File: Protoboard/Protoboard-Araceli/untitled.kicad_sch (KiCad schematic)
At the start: 23 parts, among them SW1 SW_DIP_x04, SW3 SW_Push, U1 PIC18F4550-IP, U2 HDSP-7803

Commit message: Multiplexed display
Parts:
- removed BAR1: HDSP-4830_2, Display:HDSP-4830, symbol LED:HDSP-4830_2
- removed R1, R2, R3, R4, R5, R6, R7, R8: 330, symbol Device:R
- removed R11, R12, R13, R14, R15, R16, R17: 10k, symbol Device:R
- removed R18: 470, symbol Device:R
- removed R19: 10K, symbol Device:R
- removed SW: SW_DIP_x08, symbol Switch:SW_DIP_x08
- removed SW1: SW_DIP_x04, symbol Switch:SW_DIP_x04
- removed SW3: SW_Push, symbol Switch:SW_Push
- removed U1: PIC18F4550-IP, Package_DIP:DIP-40_W15.24mm, symbol MCU_Microchip_PIC18:PIC18F4550-IP
- removed U2: HDSP-7803, Display_7Segment:HDSP-7801, symbol Display_Character:HDSP-7803
- added BAR2: HDSP-4830_2, Display:HDSP-4830, symbol LED:HDSP-4830_2
- added LEFT, RIght: HDSP-7803, Display_7Segment:HDSP-7801, symbol Display_Character:HDSP-7803
- added R10, R20, R21, R22, R23, R32, R9: 10k, symbol Device:R
- added R24, R25, R26, R27, R28, R29, R30, R31: 330, symbol Device:R
- added R33: 470, symbol Device:R
- added R34: 10K, symbol Device:R
- added SW2: SW_DIP_x04, symbol Switch:SW_DIP_x04
- added SW4: SW_DIP_x08, symbol Switch:SW_DIP_x08
- added SW5: SW_Push, symbol Switch:SW_Push
- added U4: PIC18F4550-IP, Package_DIP:DIP-40_W15.24mm, symbol MCU_Microchip_PIC18:PIC18F4550-IP
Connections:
- net +5V: now also R34.2, SW4.10, SW4.11, SW4.12, SW4.13, SW4.14, SW4.15, SW4.16, SW4.9, U4.11 (VDD)
- net GND: now also R10.2, R20.2, R21.2, R22.2, R23.2, R32.2, R9.2, SW5.2, U4.12 (VSS)
- net MCLR: now also R33.2, R34.1, SW5.1
- net PGC-5: now also R30.2, U4.39 (RB6/KBI2/PGC)
- net PGD-4: now also R31.2, U4.40 (RB7/KBI3/PGD)
- new net: BAR2.7 (A), LEFT.5 (D), R27.1, RIght.5 (D)
- new net: R27.2, U4.36 (RB3/AN9/CCP2/VPO)
- new net: BAR2.6 (A), LEFT.4 (E), R28.1, RIght.4 (E)
- new net: R28.2, U4.37 (RB4/AN11/KBI0/CSSPP)
- new net: BAR2.10 (A), LEFT.10 (A), R24.1, RIght.10 (A)
- new net: BAR2.5 (A), LEFT.2 (F), R29.1, RIght.2 (F)
- new net: BAR2.4 (A), LEFT.3 (G), R30.1, RIght.3 (G)
- new net: LEFT.6 (CC), U4.29 (P1C/SPP6/RD6)
- new net: BAR2.3 (A), LEFT.7 (DP), R31.1
- new net: BAR2.8 (A), LEFT.8 (C), R26.1, RIght.8 (C)
- new net: BAR2.9 (A), LEFT.9 (B), R25.1, RIght.9 (B)
- new net: R9.1, SW4.2, U4.14 (RA6/OSC2/CLKO)
- new net: R10.1, SW4.3, U4.7 (RA5/AN4/~{SS}/HLVDIN/C2OUT)
- new net: R20.1, SW4.4, U4.6 (RA4/T0CKI/C1OUT/RCV)
- new net: R21.1, SW4.5, U4.5 (RA3/AN3/Vref+)
- new net: R22.1, SW4.6, U4.4 (RA2/AN2/Vref-/CVref)
- new net: R23.1, SW4.7, U4.3 (RA1/AN1)
- new net: R32.1, SW4.8, U4.2 (RA0/AN0)
- new net: R26.2, U4.35 (RB2/AN8/INT2/VMO)
- new net: BAR2.11 (K), BAR2.12 (K), BAR2.13 (K), BAR2.14 (K), BAR2.15 (K), BAR2.16 (K), BAR2.17 (K), BAR2.18 (K), BAR2.19 (K), BAR2.20 (K)
- new net: R25.2, U4.34 (RB1/AN10/INT1/SCK/SCL)
- new net: R33.1, U4.1 (Vpp/~{MCLR}/RE3)
- new net: RIght.1 (CC), U4.30 (P1D/SPP7/RD7)
- new net: R24.2, U4.33 (RB0/AN12/INT0/FLT0/SDI/SDA)
- new net: R29.2, U4.38 (RB5/KBI1/PGM)
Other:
- removed sheet Mutiplexed display
- title: Protoboard Araceli -> (none)

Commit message: Last fix
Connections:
- net GND: now also SW2.6
- net at SW2.1: now also RIght.1 (CC)
- net at SW2.2: now also LEFT.6 (CC)
- net at SW2.3: now also BAR2.11 (K), BAR2.12 (K), BAR2.13 (K), BAR2.14 (K), BAR2.15 (K), BAR2.16 (K), BAR2.17 (K), BAR2.18 (K), BAR2.19 (K), BAR2.20 (K)
- net at SW2.7: now also U4.29 (P1C/SPP6/RD6)
- net at SW2.8: now also U4.30 (P1D/SPP7/RD7)
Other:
- moved on the sheet: SW2
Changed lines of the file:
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@@
+	)
+	(junction
+		(at 43.18 116.84)
+		(diameter 0)
+		(color 0 0 0 0)
 	)
 	(junction
@@
 	(wire
 		(pts
-			(xy 231.14 87.63) (xy 231.14 148.59)
-		)
-		(stroke
-			(width 0)
-			(type default)
-		)
-	)
-	(wire
-		(pts
 			(xy 54.61 111.76) (xy 114.3 111.76)
 		)
@@
 	(wire
 		(pts
+			(xy 121.92 140.97) (xy 147.32 140.97)
+		)
+		(stroke
+			(width 0)
+			(type default)
+		)
+	)
+	(wire
+		(pts
 			(xy 72.39 130.81) (xy 67.31 130.81)
 		)
@@
 	(wire
 		(pts
+			(xy 130.81 143.51) (xy 130.81 148.59)
+		)
+		(stroke
+			(width 0)
+			(type default)
+		)
+	)
+	(wire
+		(pts
 			(xy 67.31 130.81) (xy 67.31 99.06)
 		)
@@
 	(wire
 		(pts
+			(xy 162.56 146.05) (xy 171.45 146.05)
+		)
+		(stroke
+			(width 0)
+			(type default)
+		)
+	)
+	(wire
+		(pts
 			(xy 130.81 101.6) (xy 121.92 101.6)
 		)
@@
 	(wire
 		(pts
+			(xy 229.87 143.51) (xy 162.56 143.51)
+		)
+		(stroke
+			(width 0)
+			(type default)
+		)
+	)
+	(wire
+		(pts
 			(xy 101.6 99.06) (xy 114.3 99.06)
 		)
@@
 	(wire
 		(pts
-			(xy 195.58 87.63) (xy 231.14 87.63)
-		)
-		(stroke
-			(width 0)
-			(type default)
-		)
-	)
-	(wire
-		(pts
-			(xy 227.33 140.97) (xy 121.92 140.97)
-		)
-		(stroke
-			(width 0)
-			(type default)
-		)
-	)
-	(wire
-		(pts
 			(xy 99.06 133.35) (xy 99.06 101.6)
 		)
@@
 	(wire
 		(pts
+			(xy 132.08 146.05) (xy 147.32 146.05)
+		)
+		(stroke
+			(width 0)
+			(type default)
+		)
+	)
+	(wire
+		(pts
 			(xy 43.18 101.6) (xy 43.18 104.14)
 		)
@@
 	(wire
 		(pts
-			(xy 231.14 148.59) (xy 87.63 148.59)
+			(xy 43.18 116.84) (xy 43.18 151.13)
 		)
 		(stroke
@@
 	(wire
 		(pts
+			(xy 43.18 151.13) (xy 132.08 151.13)
+		)
+		(stroke
+			(width 0)
+			(type default)
+		)
+	)
+	(wire
+		(pts
 			(xy 53.34 111.76) (xy 54.61 111.76)
 		)
@@
 	(wire
 		(pts
+			(xy 195.58 87.63) (xy 229.87 87.63)
+		)
+		(stroke
+			(width 0)
+			(type default)
+		)
+	)
+	(wire
+		(pts
 			(xy 104.14 96.52) (xy 114.3 96.52)
 		)
@@
 	(wire
 		(pts
-			(xy 128.27 175.26) (xy 128.27 177.8)
-		)
-		(stroke
-			(width 0)
-			(type default)
-		)
-	)
-	(wire
-		(pts
 			(xy 147.32 114.3) (xy 147.32 123.19)
 		)
@@
 	(wire
 		(pts
+			(xy 171.45 146.05) (xy 171.45 148.59)
+		)
+		(stroke
+			(width 0)
+			(type default)
+		)
+	)
+	(wire
+		(pts
+			(xy 130.81 148.59) (xy 87.63 148.59)
+		)
+		(stroke
+			(width 0)
+			(type default)
+		)
+	)
+	(wire
+		(pts
+			(xy 147.32 143.51) (xy 130.81 143.51)
+		)
+		(stroke
+			(width 0)
+			(type default)
+		)
+	)
+	(wire
+		(pts
 			(xy 53.34 96.52) (xy 69.85 96.52)
 		)
@@
 	(wire
 		(pts
+			(xy 229.87 87.63) (xy 229.87 143.51)
+		)
+		(stroke
+			(width 0)
+			(type default)
+		)
+	)
+	(wire
+		(pts
+			(xy 132.08 151.13) (xy 132.08 146.05)
+		)
+		(stroke
+			(width 0)
+			(type default)
+		)
+	)
+	(wire
+		(pts
 			(xy 165.1 110.49) (xy 165.1 118.11)
+		)
+		(stroke
+			(width 0)
+			(type default)
+		)
+	)
+	(wire
+		(pts
+			(xy 162.56 140.97) (xy 227.33 140.97)
 		)
 		(stroke
@@
 	(symbol
 		(lib_id "power:GND")
-		(at 128.27 177.8 0)
+		(at 171.45 148.59 0)
 		(unit 1)
 		(exclude_from_sim no)
@@
 		(fields_autoplaced yes)
 		(property "Reference" "#PWR010"
-			(at 128.27 184.15 0)
+			(at 171.45 154.94 0)
 			(effects
 				(font
@@
 		)
 		(property "Value" "GND"
-			(at 128.27 182.88 0)
-			(effects
-				(font
-					(size 1.27 1.27)
-				)
+			(at 173.99 149.8599 0)
+			(effects
+				(font
+					(size 1.27 1.27)
+				)
+				(justify left)
 			)
 		)
 		(property "Footprint" ""
-			(at 128.27 177.8 0)
+			(at 171.45 148.59 0)
 			(effects
 				(font
@@
 		)
 		(property "Datasheet" ""
-			(at 128.27 177.8 0)
+			(at 171.45 148.59 0)
 			(effects
 				(font
@@
 		)
 		(property "Description" "Power symbol creates a global label with name \"GND\" , ground"
-			(at 128.27 177.8 0)
+			(at 171.45 148.59 0)
 			(effects
 				(font
@@
 	(symbol
 		(lib_id "Switch:SW_DIP_x04")
-		(at 139.7 167.64 270)
+		(at 154.94 146.05 0)
 		(unit 1)
 		(exclude_from_sim no)
@@
 		(fields_autoplaced yes)
 		(property "Reference" "SW2"
-			(at 148.59 166.3699 90)
+			(at 153.6699 137.16 90)
 			(effects
 				(font
@@
 		)
 		(property "Value" "SW_DIP_x04"
-			(at 148.59 168.9099 90)
+			(at 156.2099 137.16 90)
 			(effects
 				(font
@@
 		)
 		(property "Footprint" ""
-			(at 139.7 167.64 0)
+			(at 154.94 146.05 0)
 			(effects
 				(font
@@
 		)
 		(property "Datasheet" "~"
-			(at 139.7 167.64 0)
+			(at 154.94 146.05 0)
 			(effects
 				(font
@@
 		)
 		(property "Description" "4x DIP Switch, Single Pole Single Throw (SPST) switch, small symbol"
-			(at 139.7 167.64 0)
-			(effects
-				(font
+			(at 154.94 146.05 0)
+			(effects
+				(font

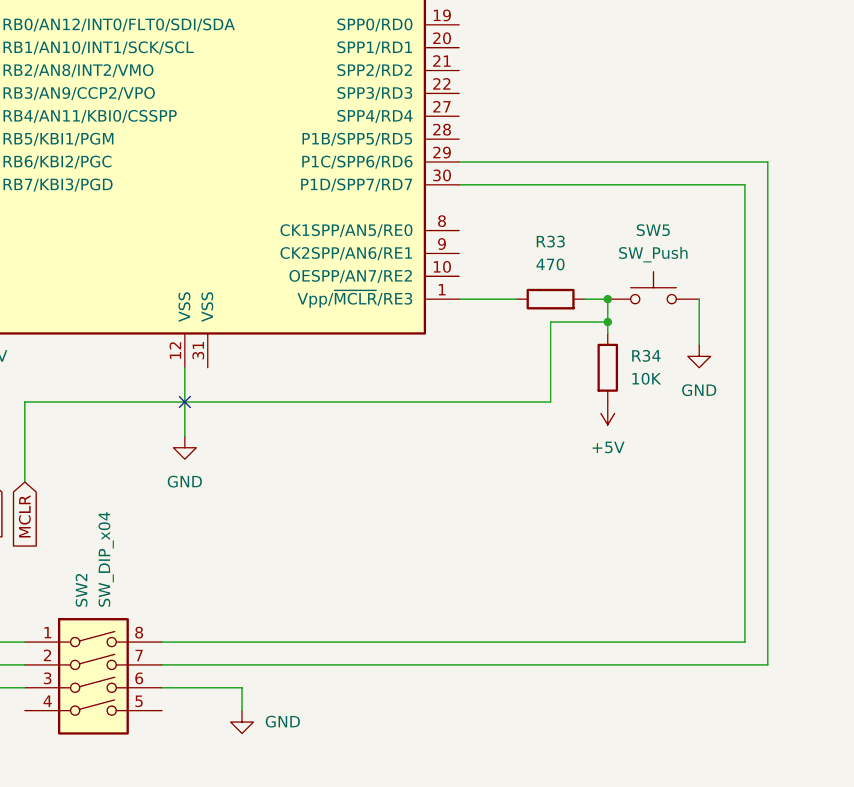
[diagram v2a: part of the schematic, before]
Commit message: safety resistors added
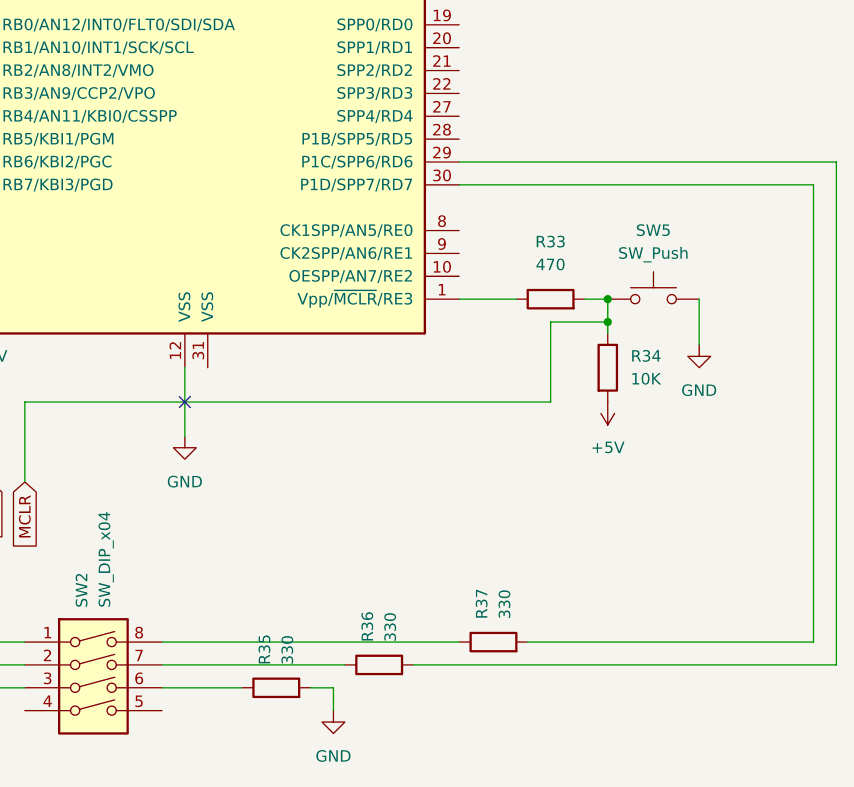
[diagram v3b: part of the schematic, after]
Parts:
- added R35, R36, R37: 330, symbol Device:R
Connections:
- net GND: now also R35.2; no longer SW2.6
- net at SW2.7: now also R36.1; no longer U4.29 (P1C/SPP6/RD6)
- net at SW2.8: now also R37.1; no longer U4.30 (P1D/SPP7/RD7)
- new net: R36.2, U4.29 (P1C/SPP6/RD6)
- new net: R35.1, SW2.6
- new net: R37.2, U4.30 (P1D/SPP7/RD7)
